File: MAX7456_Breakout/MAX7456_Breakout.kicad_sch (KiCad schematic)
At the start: 16 parts, among them J1 Conn_01x14_Socket, U1 MAX7456EUI_, Y1 27MHz

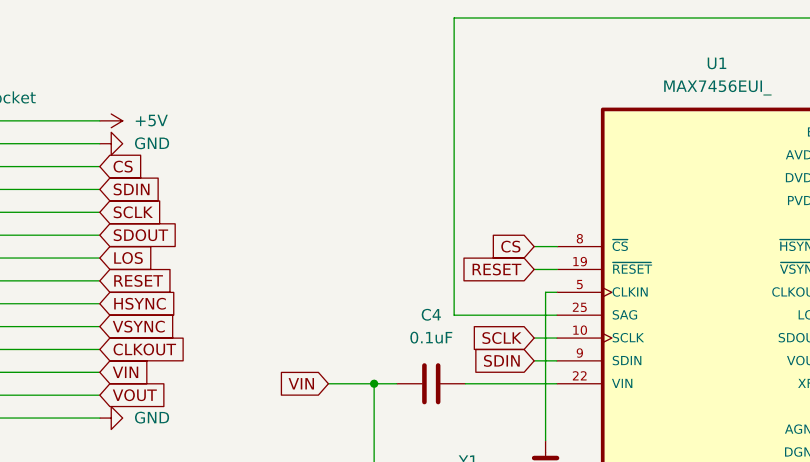
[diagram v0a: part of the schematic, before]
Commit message: Added 10k pullup on reset
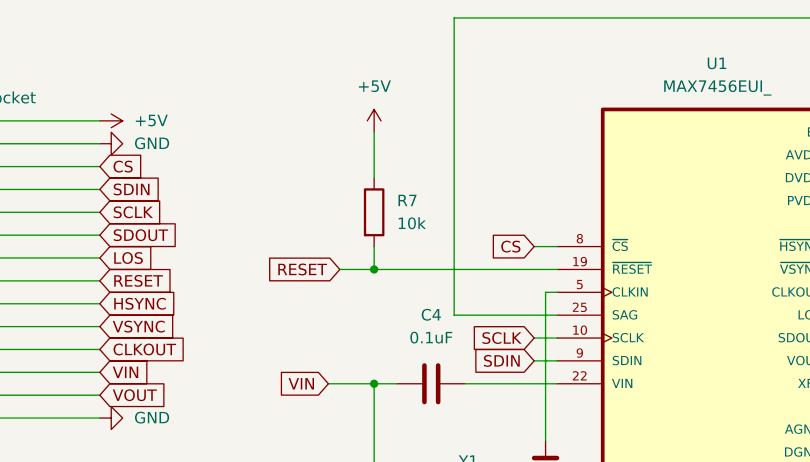
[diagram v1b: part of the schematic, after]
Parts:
- added R7: 10k, Resistor_SMD:R_0402_1005Metric_Pad0.72x0.64mm_HandSolder, symbol Device:R
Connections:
- net +5V: now also R7.1
- net RESET: now also R7.2
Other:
- title: (none) -> MAX7456 Breakout
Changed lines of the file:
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@@
 	(generator_version "8.0")
 	(paper "A4")
+	(title_block
+		(title "MAX7456 Breakout")
+	)
 	(junction
 		(at 166.37 115.57)
@@
 	)
 	(junction
+		(at 102.87 96.52)
+		(diameter 0)
+		(color 0 0 0 0)
+	)
+	(junction
 		(at 162.56 88.9)
 		(diameter 0)
@@
 	(wire
 		(pts
-			(xy 120.65 96.52) (xy 123.19 96.52)
+			(xy 99.06 96.52) (xy 102.87 96.52)
 		)
 		(stroke
@@
 	(wire
 		(pts
+			(xy 102.87 81.28) (xy 102.87 86.36)
+		)
+		(stroke
+			(width 0)
+			(type default)
+		)
+	)
+	(wire
+		(pts
 			(xy 158.75 109.22) (xy 160.02 109.22)
 		)
@@
 	(wire
 		(pts
+			(xy 102.87 96.52) (xy 123.19 96.52)
+		)
+		(stroke
+			(width 0)
+			(type default)
+		)
+	)
+	(wire
+		(pts
 			(xy 189.23 93.98) (xy 196.85 93.98)
 		)
@@
 		(pts
 			(xy 60.96 105.41) (xy 72.39 105.41)
+		)
+		(stroke
+			(width 0)
+			(type default)
+		)
+	)
+	(wire
+		(pts
+			(xy 102.87 93.98) (xy 102.87 96.52)
 		)
 		(stroke
@@
 	(global_label "RESET"
 		(shape input)
-		(at 120.65 96.52 180)
+		(at 99.06 96.52 180)
 		(fields_autoplaced yes)
 		(effects
@@
 		)
 		(property "Intersheetrefs" "${INTERSHEET_REFS}"
-			(at 111.9197 96.52 0)
+			(at 90.3297 96.52 0)
 			(effects
 				(font
@@
 					(unit 1)
 				)
+			)
+		)
+	)
+	(symbol
+		(lib_id "power:+5V")
+		(at 102.87 81.28 0)
+		(unit 1)
+		(exclude_from_sim no)
+		(in_bom yes)
+		(on_board yes)
+		(dnp no)
+		(fields_autoplaced yes)
+		(property "Reference" "#PWR09"
+			(at 102.87 85.09 0)
+			(effects
+				(font
+					(size 1.27 1.27)
+				)
+				(hide yes)
+			)
+		)
+		(property "Value" "+5V"
+			(at 102.87 76.2 0)
+			(effects
+				(font
+					(size 1.27 1.27)
+				)
+			)
+		)
+		(property "Footprint" ""
+			(at 102.87 81.28 0)
+			(effects
+				(font
+					(size 1.27 1.27)
+				)
+				(hide yes)
+			)
+		)
+		(property "Datasheet" ""
+			(at 102.87 81.28 0)
+			(effects
+				(font
+					(size 1.27 1.27)
+				)
+				(hide yes)
+			)
+		)
+		(property "Description" "Power symbol creates a global label with name \"+5V\""
+			(at 102.87 81.28 0)
+			(effects
+				(font
+					(size 1.27 1.27)
+				)
+				(hide yes)
+			)
+		)
+		(pin "1"
+		)
+		(instances
+			(project ""
+				(path "/5617f566-b420-4642-b5a1-7d4ede49c588"
+					(reference "#PWR09")
+					(unit 1)
+				)
+			)
+		)
+	)
+	(symbol
+		(lib_id "Device:R")
+		(at 102.87 90.17 0)
+		(unit 1)
+		(exclude_from_sim no)
+		(in_bom yes)
+		(on_board yes)
+		(dnp no)
+		(fields_autoplaced yes)
+		(property "Reference" "R7"
+			(at 105.41 88.8999 0)
+			(effects
+				(font
+					(size 1.27 1.27)
+				)
+				(justify left)
+			)
+		)
+		(property "Value" "10k"
+			(at 105.41 91.4399 0)
+			(effects
+				(font
+					(size 1.27 1.27)
+				)
+				(justify left)
+			)
+		)
+		(property "Footprint" "Resistor_SMD:R_0402_1005Metric_Pad0.72x0.64mm_HandSolder"
+			(at 101.092 90.17 90)
+			(effects
+				(font
+					(size 1.27 1.27)
+				)
+				(hide yes)
+			)
+		)
+		(property "Datasheet" "~"
+			(at 102.87 90.17 0)
+			(effects
+				(font
+					(size 1.27 1.27)
+				)
+				(hide yes)
+			)
+		)
+		(property "Description" "Resistor"
+			(at 102.87 90.17 0)
+			(effects
+				(font
+					(size 1.27 1.27)
+				)
+				(hide yes)
+			)
+		)
+		(pin "1"
+		)
+		(pin "2"
+		)
+		(instances
+			(project ""
+				(path "/5617f566-b420-4642-b5a1-7d4ede49c588"
+					(reference "R7")
+					(unit 1)
+				)
